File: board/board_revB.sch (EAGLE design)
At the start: 83 parts, among them IC1 MCP1703CB, Q1 ULN2003AS, Q2 ULN2003AD, Y1 8Mhz

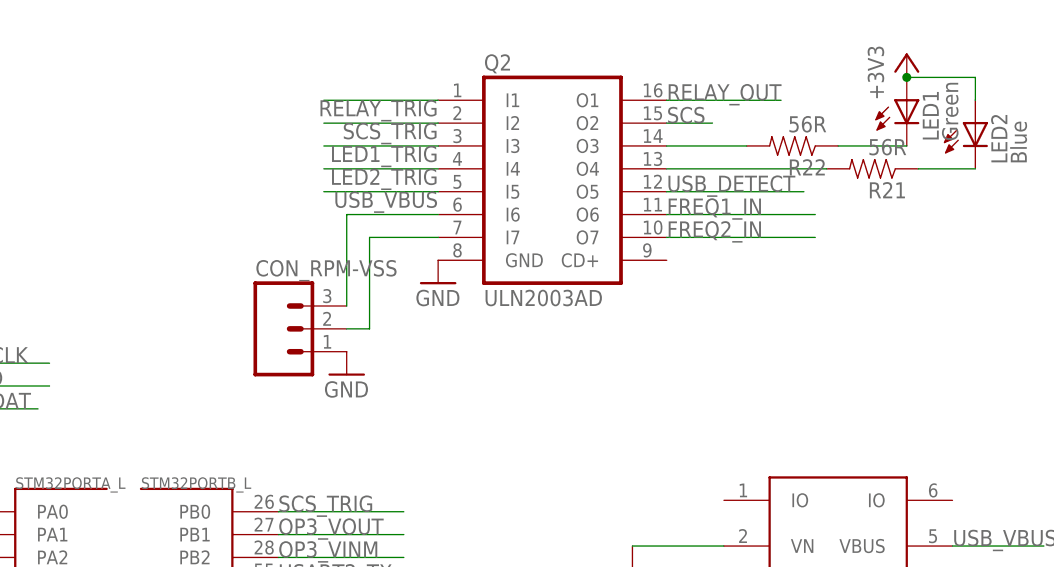
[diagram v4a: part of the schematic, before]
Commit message: [Code] Now using CCM for ISRs and time critical threads
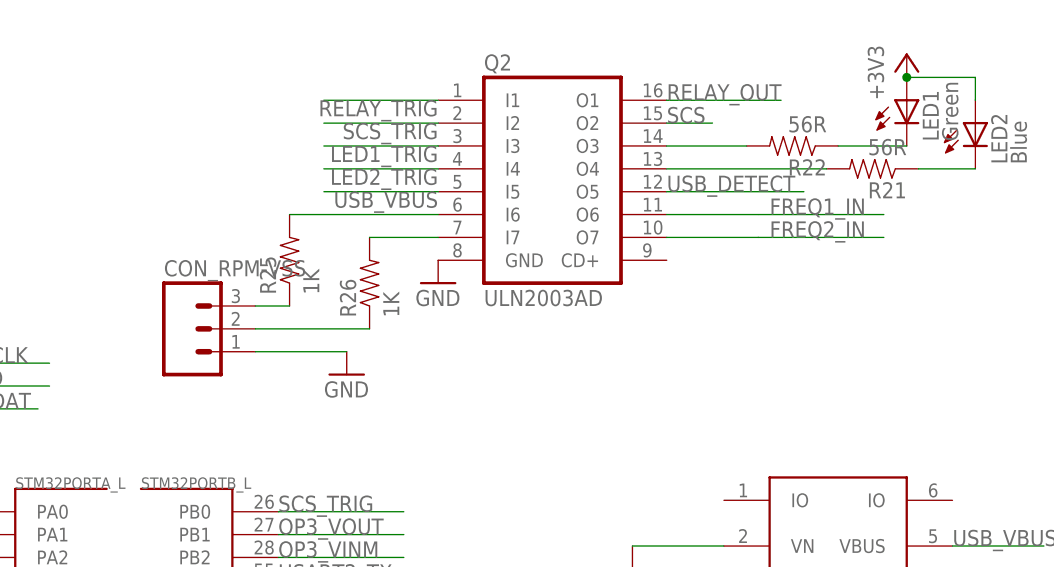
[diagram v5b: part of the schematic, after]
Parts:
- added R25, R26: 1K, SparkFun-Resistors:RESISTOR0603-RES
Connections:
- new net N$12: CON_RPM-VSS.3, R25.1
- new net N$9: Q2.I7, R26.2
- net N$16: now also R25.2; no longer CON_RPM-VSS.3
- net N$21: now also R26.1; no longer Q2.I7
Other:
- moved on the sheet: CON_RPM-VSS
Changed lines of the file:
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@@
 <setting verticaltext="up"/>
 </settings>
-<grid distance="0.1" unitdist="inch" unit="inch" style="lines" multiple="1" display="no" altdistance="0.01" altunitdist="inch" altunit="inch"/>
+<grid distance="0.05" unitdist="inch" unit="inch" style="lines" multiple="1" display="yes" altdistance="0.005" altunitdist="inch" altunit="inch"/>
 <layers>
 <layer number="1" name="Top" color="4" fill="1" visible="no" active="no"/>
@@
 <part name="P+11" library="supply1" deviceset="+5V" device=""/>
 <part name="IC1" library="linear" deviceset="MCP1703" device="CB"/>
+<part name="R25" library="SparkFun-Resistors" deviceset="RESISTOR" device="0603-RES" value="1K"/>
+<part name="R26" library="SparkFun-Resistors" deviceset="RESISTOR" device="0603-RES" value="1K"/>
 </parts>
 <sheets>
@@
 <instance part="GND16" gate="1" x="63.5" y="74.93"/>
 <instance part="D2" gate="G$1" x="73.66" y="151.13" rot="R90"/>
-<instance part="CON_RPM-VSS" gate="G$1" x="176.53" y="158.75"/>
+<instance part="CON_RPM-VSS" gate="G$1" x="166.37" y="158.75"/>
 <instance part="GND17" gate="1" x="184.15" y="153.67"/>
 <instance part="C6" gate="G$1" x="114.3" y="113.03"/>
@@
 <instance part="P+11" gate="1" x="54.61" y="118.11"/>
 <instance part="IC1" gate="G$1" x="53.34" y="193.04"/>
+<instance part="R25" gate="G$1" x="177.8" y="166.37" rot="R90"/>
+<instance part="R26" gate="G$1" x="186.69" y="163.83" rot="R90"/>
 </instances>
 <busses>
@@
 <pinref part="CON_RPM-VSS" gate="G$1" pin="1"/>
 <pinref part="GND17" gate="1" pin="GND"/>
+<wire x1="173.99" y1="156.21" x2="184.15" y2="156.21" width="0.1524" layer="91"/>
 </segment>
 <segment>
@@
 <net name="FREQ2_IN" class="0">
 <segment>
-<pinref part="Q2" gate="A" pin="O7"/>
-<wire x1="219.71" y1="168.91" x2="236.22" y2="168.91" width="0.1524" layer="91"/>
-<label x="219.71" y="168.91" size="1.778" layer="95"/>
-</segment>
-<segment>
 <pinref part="STM32" gate="PORTC_L" pin="PC7"/>
 <wire x1="142.24" y1="69.85" x2="132.08" y2="69.85" width="0.1524" layer="91"/>
 <label x="142.24" y="69.85" size="1.778" layer="95" rot="R180"/>
 </segment>
+<segment>
+<wire x1="229.87" y1="168.91" x2="243.84" y2="168.91" width="0.1524" layer="91"/>
+<label x="231.14" y="168.91" size="1.778" layer="95"/>
+<pinref part="Q2" gate="A" pin="O7"/>
+<wire x1="229.87" y1="168.91" x2="219.71" y2="168.91" width="0.1524" layer="91"/>
+</segment>
 </net>
 <net name="FREQ1_IN" class="0">
-<segment>
-<pinref part="Q2" gate="A" pin="O6"/>
-<wire x1="219.71" y1="171.45" x2="236.22" y2="171.45" width="0.1524" layer="91"/>
-<label x="219.71" y="171.45" size="1.778" layer="95"/>
-</segment>
 <segment>
 <pinref part="STM32" gate="PORTC_L" pin="PC6"/>
@@
 <label x="142.24" y="72.39" size="1.778" layer="95" rot="R180"/>
 </segment>
+<segment>
+<wire x1="229.87" y1="171.45" x2="243.84" y2="171.45" width="0.1524" layer="91"/>
+<label x="231.14" y="171.45" size="1.778" layer="95"/>
+<pinref part="Q2" gate="A" pin="O6"/>
+<wire x1="229.87" y1="171.45" x2="219.71" y2="171.45" width="0.1524" layer="91"/>
+</segment>
 </net>
 <net name="N$16" class="0">
 <segment>
-<pinref part="CON_RPM-VSS" gate="G$1" pin="3"/>
-<wire x1="184.15" y1="161.29" x2="184.15" y2="171.45" width="0.1524" layer="91"/>
 <pinref part="Q2" gate="A" pin="I6"/>
-<wire x1="184.15" y1="171.45" x2="194.31" y2="171.45" width="0.1524" layer="91"/>
+<wire x1="177.8" y1="171.45" x2="194.31" y2="171.45" width="0.1524" layer="91"/>
+<pinref part="R25" gate="G$1" pin="2"/>
 </segment>
 </net>
 <net name="N$21" class="0">
 <segment>
-<pinref part="Q2" gate="A" pin="I7"/>
-<wire x1="194.31" y1="168.91" x2="186.69" y2="168.91" width="0.1524" layer="91"/>
-<wire x1="186.69" y1="168.91" x2="186.69" y2="158.75" width="0.1524" layer="91"/>
 <pinref part="CON_RPM-VSS" gate="G$1" pin="2"/>
-<wire x1="186.69" y1="158.75" x2="184.15" y2="158.75" width="0.1524" layer="91"/>
+<wire x1="186.69" y1="158.75" x2="173.99" y2="158.75" width="0.1524" layer="91"/>
+<pinref part="R26" gate="G$1" pin="1"/>
 </segment>
 </net>
@@
 </segment>
 </net>
+<net name="N$9" class="0">
+<segment>
+<pinref part="Q2" gate="A" pin="I7"/>
+<wire x1="194.31" y1="168.91" x2="186.69" y2="168.91" width="0.1524" layer="91"/>
+<pinref part="R26" gate="G$1" pin="2"/>
+</segment>
+</net>
+<net name="N$12" class="0">
+<segment>
+<pinref part="CON_RPM-VSS" gate="G$1" pin="3"/>
+<pinref part="R25" gate="G$1" pin="1"/>
+<wire x1="173.99" y1="161.29" x2="177.8" y2="161.29" width="0.1524" layer="91"/>
+</segment>
+</net>

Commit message: [Board] Updates
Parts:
- added ESP: ESP8266, misc:ESP8266
- IC_FRAM: value 25LC080SN -> FM25L04B
- renumbered IC_EE to IC_FRAM
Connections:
- net GND: now also IC_OPAD.+IN, IC_OPAD.-IN
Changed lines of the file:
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@@
 <part name="+3V16" library="supply1" deviceset="+3V3" device=""/>
 <part name="+3V18" library="supply1" deviceset="+3V3" device=""/>
-<part name="IC_EE" library="microchip" deviceset="25*" device="SN" technology="LC080"/>
+<part name="IC_FRAM" library="microchip" deviceset="25*" device="SN" technology="LC080" value="FM25L04B"/>
 <part name="GND26" library="supply1" deviceset="GND" device=""/>
 <part name="P+7" library="supply1" deviceset="+5V" device=""/>
@@
 <part name="R25" library="SparkFun-Resistors" deviceset="RESISTOR" device="0603-RES" value="1K"/>
 <part name="R26" library="SparkFun-Resistors" deviceset="RESISTOR" device="0603-RES" value="1K"/>
+<part name="GND31" library="supply1" deviceset="GND" device=""/>
+<part name="ESP" library="misc" deviceset="ESP8266" device=""/>
 </parts>
 <sheets>
@@
 <instance part="+3V16" gate="G$1" x="243.84" y="33.02"/>
 <instance part="+3V18" gate="G$1" x="240.03" y="16.51"/>
-<instance part="IC_EE" gate="G$1" x="256.54" y="22.86"/>
+<instance part="IC_FRAM" gate="G$1" x="256.54" y="22.86"/>
 <instance part="IC_OPA" gate="D" x="39.37" y="148.59"/>
 <instance part="GND26" gate="1" x="53.34" y="182.88"/>
@@
 <instance part="R25" gate="G$1" x="177.8" y="166.37" rot="R90"/>
 <instance part="R26" gate="G$1" x="186.69" y="163.83" rot="R90"/>
+<instance part="GND31" gate="1" x="31.75" y="143.51"/>
+<instance part="ESP" gate="G$1" x="318.77" y="27.94"/>
 </instances>
 <busses>
@@
 <segment>
 <pinref part="GND22" gate="1" pin="GND"/>
-<pinref part="IC_EE" gate="G$1" pin="GND"/>
+<pinref part="IC_FRAM" gate="G$1" pin="GND"/>
 </segment>
 <segment>
@@
 <pinref part="IC1" gate="G$1" pin="GND"/>
 <pinref part="GND26" gate="1" pin="GND"/>
+</segment>
+<segment>
+<pinref part="IC_OPA" gate="D" pin="+IN"/>
+<pinref part="IC_OPA" gate="D" pin="-IN"/>
+<wire x1="31.75" y1="151.13" x2="31.75" y2="146.05" width="0.1524" layer="91"/>
+<pinref part="GND31" gate="1" pin="GND"/>
+<junction x="31.75" y="146.05"/>
 </segment>
 </net>
@@
 <pinref part="STM32" gate="AN_POWER" pin="VDDA"/>
 <wire x1="177.8" y1="25.4" x2="190.5" y2="25.4" width="0.1524" layer="91"/>
-<pinref part="STM32" gate="AN_POWER" pin="VBAT"/>
-<wire x1="177.8" y1="35.56" x2="190.5" y2="35.56" width="0.1524" layer="91"/>
 <wire x1="190.5" y1="35.56" x2="190.5" y2="25.4" width="0.1524" layer="91"/>
 <pinref part="+3V2" gate="G$1" pin="+3V3"/>
+<pinref part="STM32" gate="AN_POWER" pin="VBAT"/>
+<wire x1="177.8" y1="35.56" x2="184.15" y2="35.56" width="0.1524" layer="91"/>
+<wire x1="184.15" y1="35.56" x2="190.5" y2="35.56" width="0.1524" layer="91"/>
 <junction x="190.5" y="35.56"/>
 </segment>
@@
 <wire x1="240.03" y1="13.97" x2="243.84" y2="13.97" width="0.1524" layer="91"/>
 <wire x1="243.84" y1="13.97" x2="243.84" y2="17.78" width="0.1524" layer="91"/>
-<pinref part="IC_EE" gate="G$1" pin="!HOLD"/>
+<pinref part="IC_FRAM" gate="G$1" pin="!HOLD"/>
 </segment>
 <segment>
 <pinref part="+3V6" gate="G$1" pin="+3V3"/>
-<pinref part="IC_EE" gate="G$1" pin="VCC"/>
+<pinref part="IC_FRAM" gate="G$1" pin="VCC"/>
 </segment>
 <segment>
 <pinref part="+3V16" gate="G$1" pin="+3V3"/>
-<pinref part="IC_EE" gate="G$1" pin="!WP"/>
+<pinref part="IC_FRAM" gate="G$1" pin="!WP"/>
 </segment>
 </net>
@@
 <wire x1="243.84" y1="22.86" x2="232.41" y2="22.86" width="0.1524" layer="91"/>
 <label x="243.84" y="22.86" size="1.778" layer="95" rot="R180"/>
-<pinref part="IC_EE" gate="G$1" pin="SI"/>
+<pinref part="IC_FRAM" gate="G$1" pin="SI"/>
 </segment>
 </net>
@@
 <wire x1="271.78" y1="22.86" x2="283.21" y2="22.86" width="0.1524" layer="91"/>
 <label x="271.78" y="22.86" size="1.778" layer="95"/>
-<pinref part="IC_EE" gate="G$1" pin="SO"/>
+<pinref part="IC_FRAM" gate="G$1" pin="SO"/>
 </segment>
 </net>
@@
 <wire x1="243.84" y1="20.32" x2="232.41" y2="20.32" width="0.1524" layer="91"/>
 <label x="243.84" y="20.32" size="1.778" layer="95" rot="R180"/>
-<pinref part="IC_EE" gate="G$1" pin="SCK"/>
+<pinref part="IC_FRAM" gate="G$1" pin="SCK"/>
 </segment>
 </net>
@@
 <label x="243.84" y="25.4" size="1.778" layer="95" rot="R180"/>
 <wire x1="232.41" y1="25.4" x2="243.84" y2="25.4" width="0.1524" layer="91"/>
-<pinref part="IC_EE" gate="G$1" pin="!CS"/>
-</segment>
-</net>
+<pinref part="IC_FRAM" gate="G$1" pin="!CS"/>
+</segment>
+</net>

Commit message: [code] updated ChibiOS
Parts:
- removed ESP: ESP8266, misc:ESP8266
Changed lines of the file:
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@@
 <?xml version="1.0" encoding="utf-8"?>
 <!DOCTYPE eagle SYSTEM "eagle.dtd">
-<eagle version="7.1.0">
+<eagle version="7.3.0">
 <drawing>
 <settings>
@@
 <setting verticaltext="up"/>
 </settings>
-<grid distance="0.05" unitdist="inch" unit="inch" style="lines" multiple="1" display="yes" altdistance="0.005" altunitdist="inch" altunit="inch"/>
+<grid distance="0.1" unitdist="inch" unit="inch" style="lines" multiple="1" display="no" altdistance="0.01" altunitdist="inch" altunit="inch"/>
 <layers>
 <layer number="1" name="Top" color="4" fill="1" visible="no" active="no"/>
@@
 <part name="R26" library="SparkFun-Resistors" deviceset="RESISTOR" device="0603-RES" value="1K"/>
 <part name="GND31" library="supply1" deviceset="GND" device=""/>
-<part name="ESP" library="misc" deviceset="ESP8266" device=""/>
 </parts>
 <sheets>
@@
 <instance part="R26" gate="G$1" x="186.69" y="163.83" rot="R90"/>
 <instance part="GND31" gate="1" x="31.75" y="143.51"/>
-<instance part="ESP" gate="G$1" x="318.77" y="27.94"/>
 </instances>
 <busses>

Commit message: [Board] Working on Rev B
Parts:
- removed C22, C9: 100nF, SparkFun-Capacitors:CAP0603-CAP
- removed Q1: ULN2003AS, misc:ULN2003AS
- removed R18, R9: 4.7K, SparkFun-Resistors:RESISTOR0603-RES
- added C10, C11, C12, C13: 100nF, SparkFun-Capacitors:CAP0603-CAP
- added U1: MAX202, SparkFun-DigitalIC:MAX232TSSOP
- CON_AN, CON_KNK, CON_PWR, CON_RPM-VSS: device SparkFun-Connectors:M03PTH -> SparkFun-Connectors:M03LOCK
- CON_CAN, CON_K-LINE, CON_UART1, CON_UART2: value M02PTH -> M02LOCK; device SparkFun-Connectors:M02PTH -> SparkFun-Connectors:M02LOCK
- D6: device SparkFun-DiscreteSemi:DIODESMA -> SparkFun-DiscreteSemi:DIODESOD
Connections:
- new net N$20: C11.2, U1.C2+
- new net N$22: C11.1, U1.C2-
- new net N$23: C10.1, U1.C1-
- new net N$26: C10.2, U1.C1+
- new net N$27: C12.2, U1.V-
- new net N$29: C13.2, U1.V+
- net +12V: no longer R18.2, R9.2
- net +3V3: now also C13.1, U1.VCC
- net BUT1: no longer C22.1
- net BUT2: no longer C9.1
- net GND: now also C12.1, U1.GND; no longer C22.2, C9.2, Q1.GND
- net UART2_RXD_OUT: now also U1.R1IN; no longer Q1.I3
- net UART2_TXD_OUT: now also U1.T1OUT; no longer Q1.O5, R9.1
- net UART3_RXD_OUT: now also U1.R2IN; no longer Q1.I1
- net UART3_TXD_OUT: now also U1.T2OUT; no longer Q1.O7, R18.1
- net USART2_RX: now also U1.R1OUT; no longer Q1.O3
- net USART2_TX: now also U1.T1IN; no longer Q1.I5
- net USART3_RX: now also U1.R2OUT; no longer Q1.O1
- net USART3_TX: now also U1.T2IN; no longer Q1.I7
